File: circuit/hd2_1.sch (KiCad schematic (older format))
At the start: 48 parts, among them IC1 LP2950-3V3, IC2 GAL16V8, IC3 74HCT245N, IC4 7404N, IC5 MAX232, IC6 74HC595, IC7 DS1307, IC8 2764, J1 MICROSD-9P, J2 SDMMC06132, Q1 BS170, X1 M09?SHP

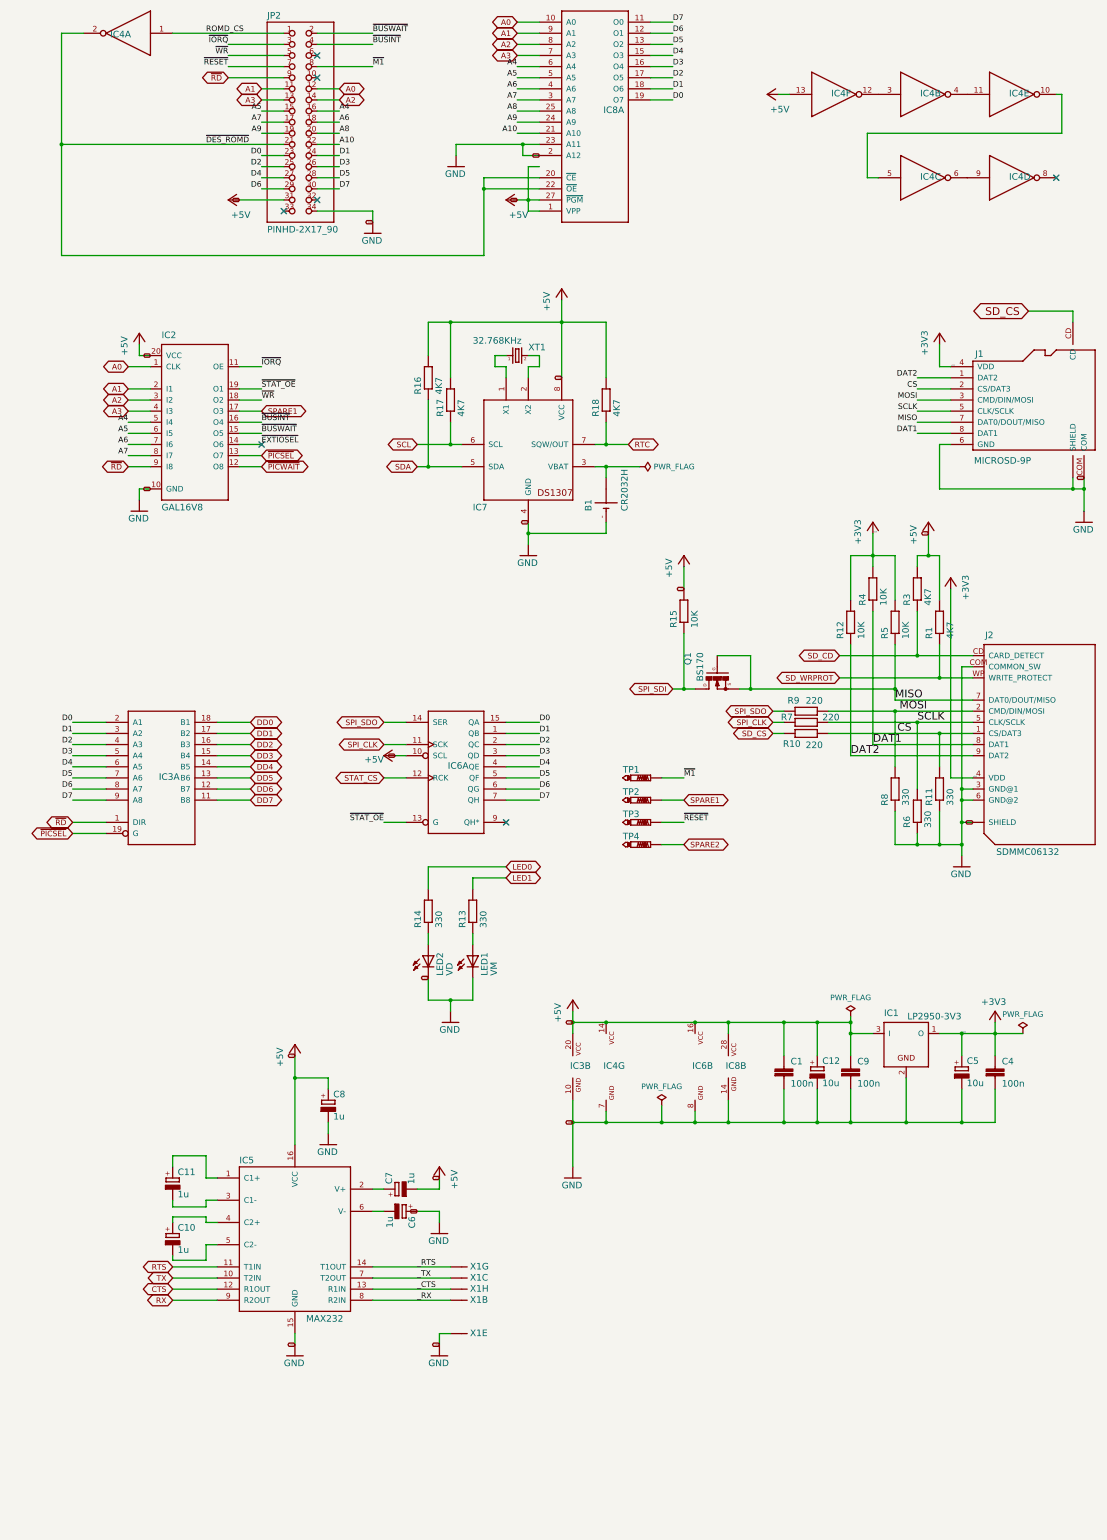
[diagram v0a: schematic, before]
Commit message: Adicionados capacitores de desacoplamento nos CIs
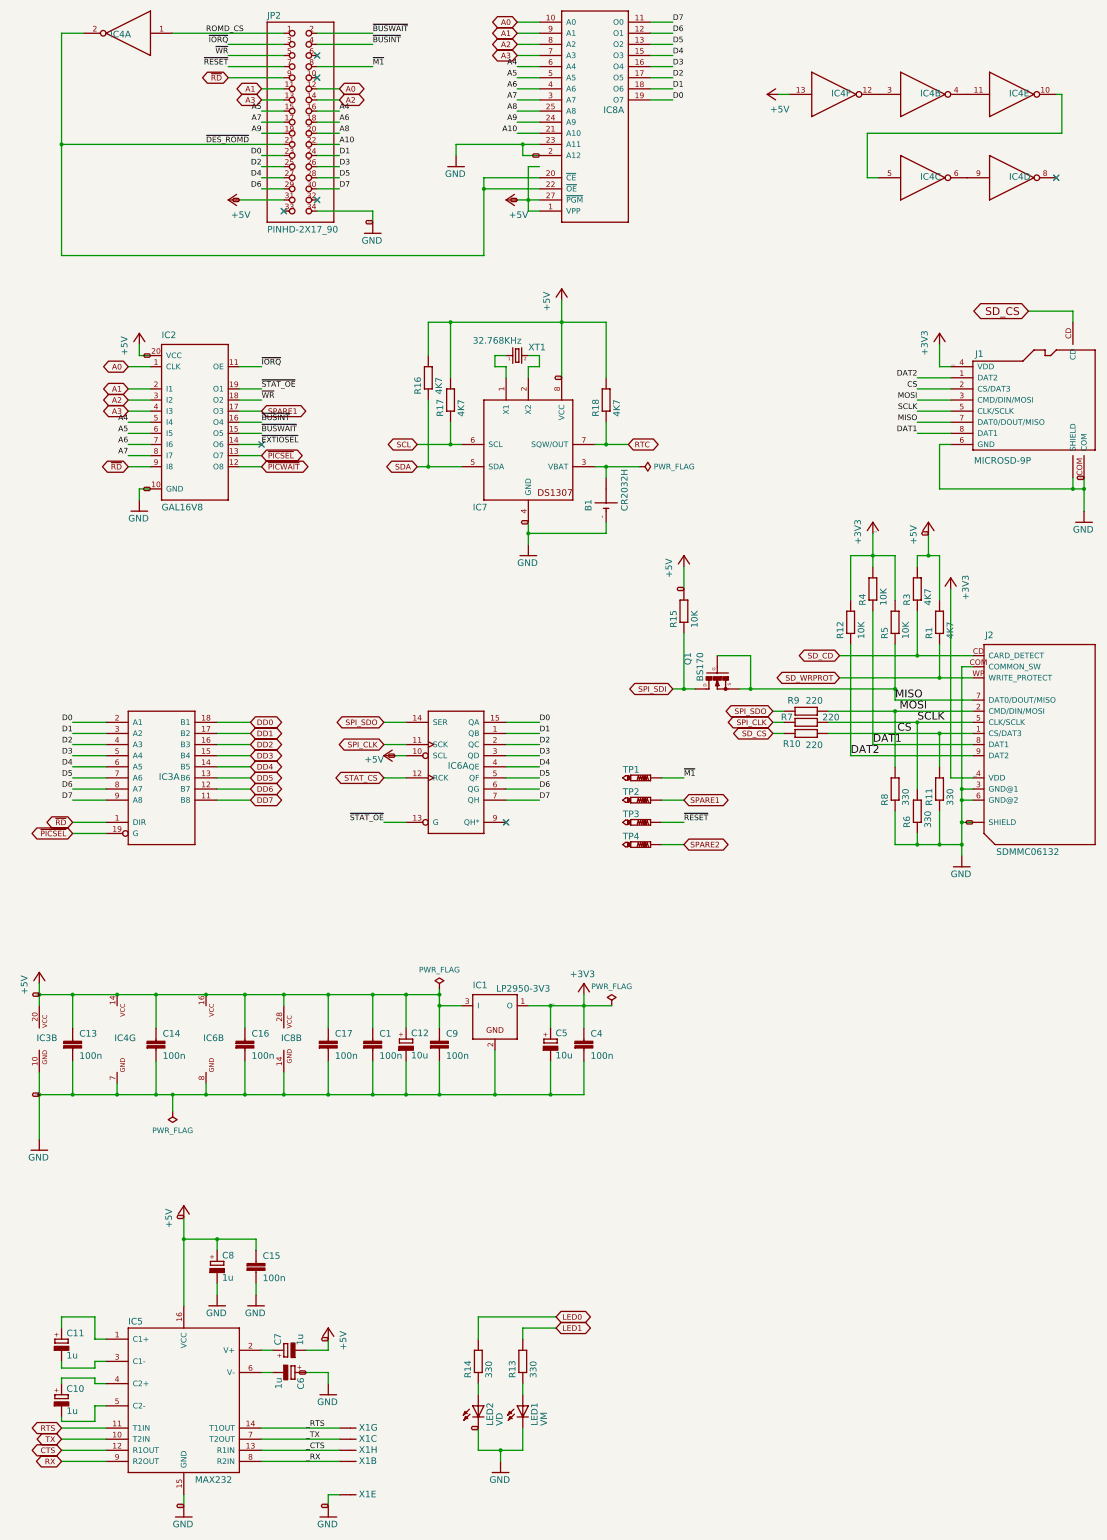
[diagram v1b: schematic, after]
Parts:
- added C13, C14, C15, C16, C17: 100n, hd2:C050-024X044, symbol hd2-eagle-import:C-EU050-024X044
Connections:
- net +5V: now also C13.1, C14.1, C15.1, C16.1, C17.1
- net GND: now also C13.2, C14.2, C16.2, C17.2
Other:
- moved on the sheet: C1, C10, C11, C12, C4, C5, C6, C7, C8, C9, IC1, IC3B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
